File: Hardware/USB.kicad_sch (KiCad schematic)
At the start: 24 parts, among them Q1 MBT3904DW1, U3 CH340C, U9 USB251xB, Y3 24MHz

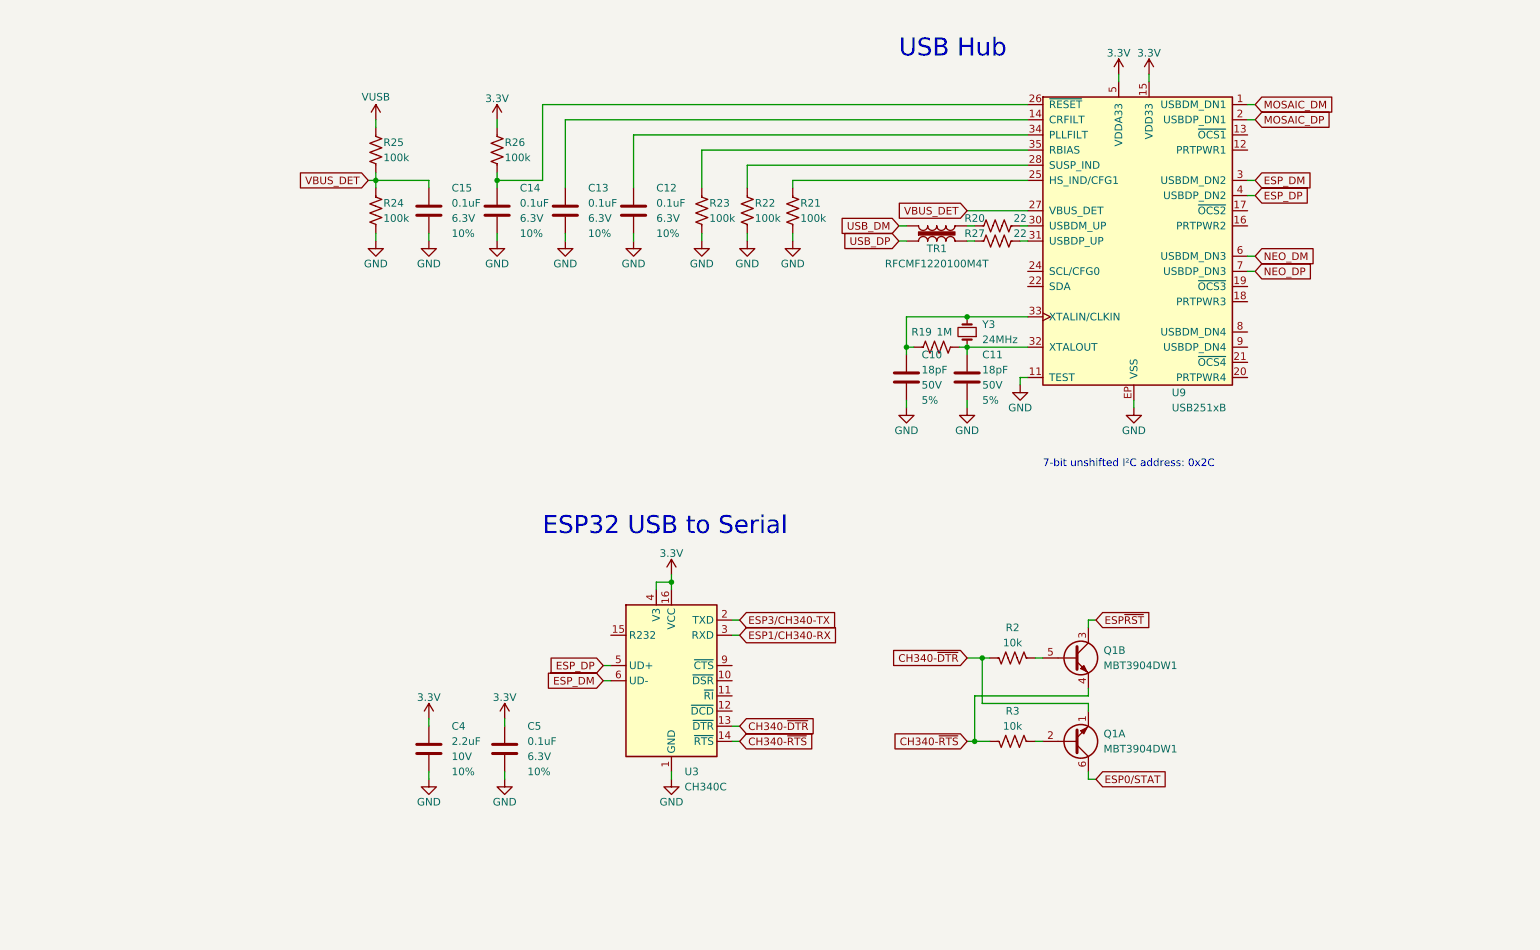
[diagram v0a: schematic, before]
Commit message: Schematic updates
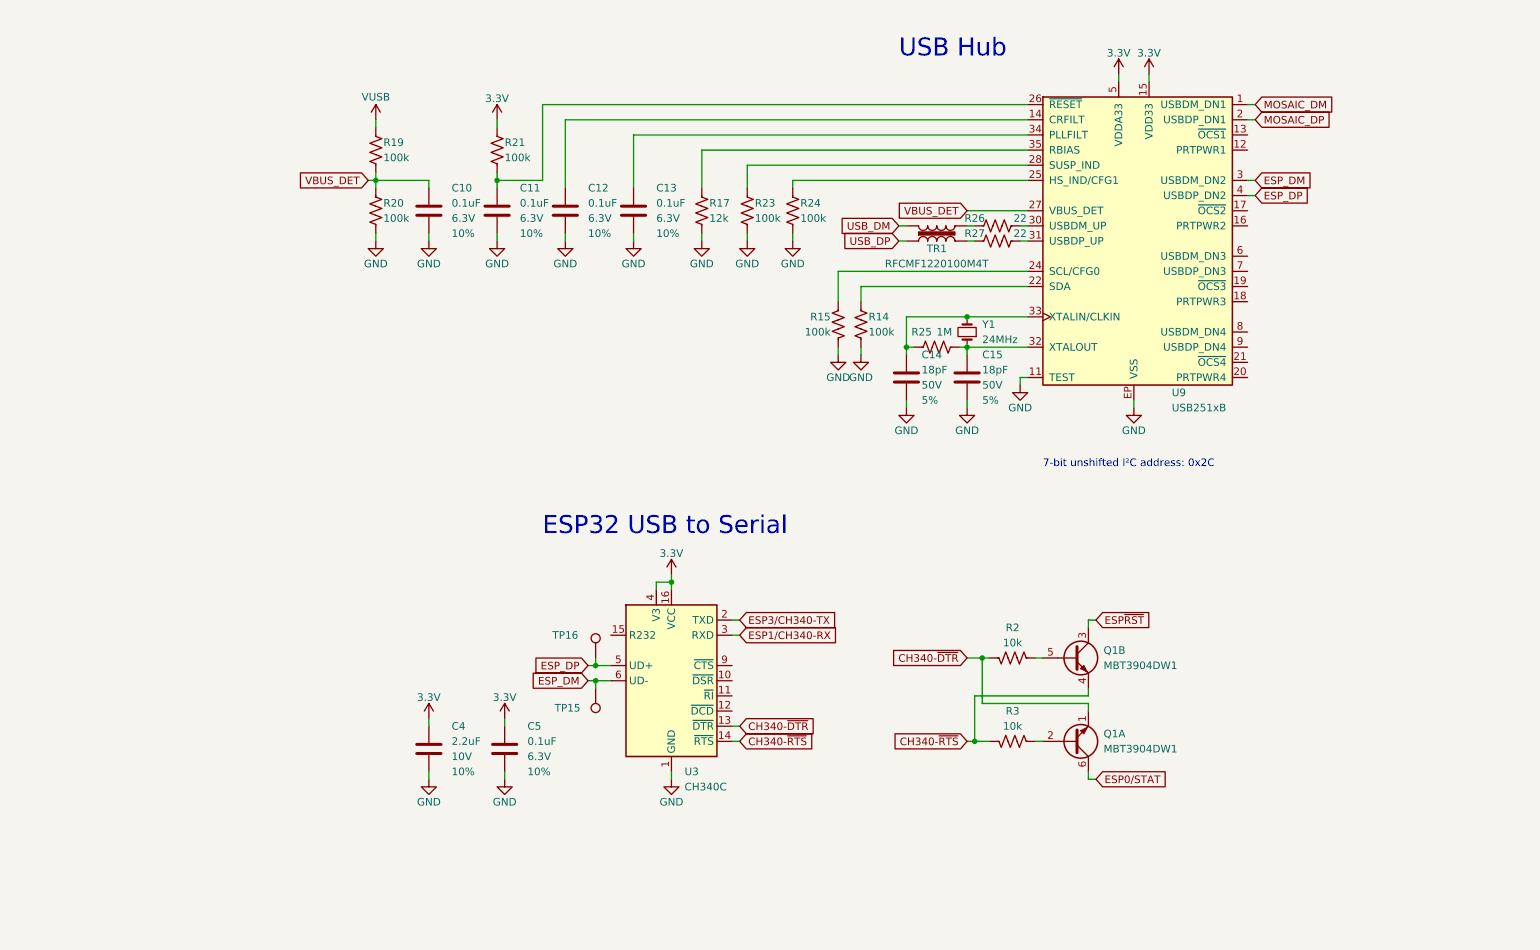
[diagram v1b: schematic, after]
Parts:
- removed R23: 100k, SparkFun-Resistor:R_0402_1005Metric, symbol SparkFun-Resistor:100k_0402
- added R14, R15: 100k, SparkFun-Resistor:R_0402_1005Metric, symbol SparkFun-Resistor:100k_0402
- added R17: 12k, SparkFun-Resistor:R_0402_1005Metric, symbol SparkFun-Resistor:12k_0402
- added TP15, TP16: PTH, SparkFun-Connector:1X01, symbol SparkFun-Connector:TestPoint_PTH
- renumbered C15 to C10, C14 to C11, C13 to C12, C12 to C13, C10 to C14, C11 to C15, R25 to R19, R24 to R20, R26 to R21, R22 to R23, R21 to R24, R19 to R25, R20 to R26, Y3 to Y1
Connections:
- net ESP_DM: now also TP15.1
- net ESP_DP: now also TP16.1
- net GND: now also R14.2, R15.2, R17.1
- net at U9.35 (RBIAS): now also R17.2
- net at U9.22 (SDA): now also R14.1
- net at U9.24 (SCL/CFG0): now also R15.1
- net NEO_DM: no longer names the net of U9.6 (USBDM_DN3)
- net NEO_DP: no longer names the net of U9.7 (USBDP_DN3)

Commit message: Ready for airwire review
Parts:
- Y1: PROD_ID XTAL- -> XTAL-14845
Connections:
- net ESP0/STAT renamed ESP0/BOOT
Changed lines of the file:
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@@
     )
   )
-  (global_label "ESP0{slash}STAT" (shape input) (at 194.31 146.05 0) (fields_autoplaced)
+  (global_label "ESP0{slash}BOOT" (shape input) (at 194.31 146.05 0) (fields_autoplaced)
     (effects (font (size 1.27 1.27)) (justify left))
     (property "Intersheetrefs" "${INTERSHEET_REFS}" (at 207.697 146.05 0)
@@
       (effects (font (size 1.27 1.27)) hide)
     )
-    (property "PROD_ID" "XTAL-" (at 182.88 71.12 0)
-      (effects (font (size 1.27 1.27)) hide)
-    )
+    (property "PROD_ID" "XTAL-14845" (at 182.88 71.12 0)
+      (effects (font (size 1.27 1.27)) hide)
+    )

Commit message: Work in progress...
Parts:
- removed TP15, TP16: PTH, SparkFun-Connector:1X01, symbol SparkFun-Connector:TestPoint_PTH
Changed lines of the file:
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@@
   (junction (at 93.98 45.72) (diameter 0) (color 0 0 0 0)
   )
-  (junction (at 110.49 129.54) (diameter 0) (color 0 0 0 0)
-  )
   (junction (at 173.99 139.7) (diameter 0) (color 0 0 0 0)
   )
@@
   (junction (at 162.56 73.66) (diameter 0) (color 0 0 0 0)
   )
-  (junction (at 110.49 127) (diameter 0) (color 0 0 0 0)
-  )
   (junction (at 123.19 113.03) (diameter 0) (color 0 0 0 0)
   )
@@
     (stroke (width 0) (type default))
   )
-  (wire (pts (xy 110.49 125.73) (xy 110.49 127))
-    (stroke (width 0) (type default))
-  )
   (wire (pts (xy 182.88 38.1) (xy 116.84 38.1))
     (stroke (width 0) (type default))
@@
     (stroke (width 0) (type default))
   )
-  (wire (pts (xy 110.49 129.54) (xy 113.03 129.54))
-    (stroke (width 0) (type default))
-  )
   (wire (pts (xy 82.55 137.16) (xy 82.55 135.89))
     (stroke (width 0) (type default))
@@
     (stroke (width 0) (type default))
   )
-  (wire (pts (xy 109.22 127) (xy 110.49 127))
-    (stroke (width 0) (type default))
-  )
   (wire (pts (xy 181.61 78.74) (xy 181.61 80.01))
     (stroke (width 0) (type default))
@@
     (stroke (width 0) (type default))
   )
-  (wire (pts (xy 109.22 129.54) (xy 110.49 129.54))
+  (wire (pts (xy 111.76 129.54) (xy 113.03 129.54))
     (stroke (width 0) (type default))
   )
@@
     (stroke (width 0) (type default))
   )
-  (wire (pts (xy 110.49 129.54) (xy 110.49 130.81))
-    (stroke (width 0) (type default))
-  )
-  (wire (pts (xy 110.49 127) (xy 113.03 127))
+  (wire (pts (xy 111.76 127) (xy 113.03 127))
     (stroke (width 0) (type default))
   )
@@
     )
   )
-  (global_label "ESP_DM" (shape input) (at 109.22 129.54 180) (fields_autoplaced)
+  (global_label "ESP_DM" (shape input) (at 111.76 129.54 180) (fields_autoplaced)
     (effects (font (size 1.27 1.27)) (justify right))
-    (property "Intersheetrefs" "${INTERSHEET_REFS}" (at 98.9173 129.54 0)
+    (property "Intersheetrefs" "${INTERSHEET_REFS}" (at 101.4573 129.54 0)
       (effects (font (size 1.27 1.27)) (justify right) hide)
     )
   )
-  (global_label "ESP_DP" (shape input) (at 109.22 127 180) (fields_autoplaced)
+  (global_label "ESP_DP" (shape input) (at 111.76 127 180) (fields_autoplaced)
     (effects (font (size 1.27 1.27)) (justify right))
-    (property "Intersheetrefs" "${INTERSHEET_REFS}" (at 99.0987 127 0)
+    (property "Intersheetrefs" "${INTERSHEET_REFS}" (at 101.6387 127 0)
       (effects (font (size 1.27 1.27)) (justify right) hide)
     )
@@
         (path "/e3dd3ae4-244d-4cba-9cca-5d2abf83f29a/0cda3e5b-c4bb-4a16-94d7-679fa3b0b0b8"
           (reference "C5") (unit 1)
-        )
-      )
-    )
-  )
-  (symbol (lib_id "SparkFun-Connector:TestPoint_PTH") (at 110.49 130.81 180) (unit 1)
-    (in_bom yes) (on_board yes) (dnp no) (fields_autoplaced)
-    (property "Reference" "TP15" (at 107.95 134.112 0)
-      (effects (font (size 1.27 1.27)) (justify left))
-    )
-    (property "Value" "PTH" (at 110.49 127 0)
-      (effects (font (size 1.27 1.27)) hide)
-    )
-    (property "Footprint" "SparkFun-Connector:1X01" (at 111.76 124.46 0)
-      (effects (font (size 1.27 1.27)) hide)
-    )
-    (property "Datasheet" "~" (at 110.49 123.19 0)
-      (effects (font (size 1.27 1.27)) hide)
-    )
-    (pin "1")
-    (instances
-      (project "SparkFun_RTK_Facet_mosaic"
-        (path "/e3dd3ae4-244d-4cba-9cca-5d2abf83f29a/0cda3e5b-c4bb-4a16-94d7-679fa3b0b0b8"
-          (reference "TP15") (unit 1)
         )
       )
@@
         )
       )
-    )
-  )
-  (symbol (lib_id "SparkFun-Connector:TestPoint_PTH") (at 110.49 125.73 0) (unit 1)
-    (in_bom yes) (on_board yes) (dnp no)
-    (property "Reference" "TP16" (at 105.41 121.92 0)
-      (effects (font (size 1.27 1.27)))
-    )
-    (property "Value" "PTH" (at 110.49 129.54 0)
-      (effects (font (size 1.27 1.27)) hide)
-    )
-    (property "Footprint" "SparkFun-Connector:1X01" (at 109.22 132.08 0)
-      (effects (font (size 1.27 1.27)) hide)
-    )
-    (property "Datasheet" "~" (at 110.49 133.35 0)
-      (effects (font (size 1.27 1.27)) hide)
-    )
-    (pin "1")
-    (instances
-      (project "SparkFun_RTK_Facet_mosaic"
-        (path "/e3dd3ae4-244d-4cba-9cca-5d2abf83f29a/0cda3e5b-c4bb-4a16-94d7-679fa3b0b0b8"
-          (reference "TP16") (unit 1)
-        )
-      )

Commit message: Routed
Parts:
- added TP19, TP20: 1.0mm, SparkFun-Connector:TestPoint-1.0mm, symbol SparkFun-Connector:TestPoint_1.0mm
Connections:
- net USB_DM: now also TP19.1
- net USB_DP: now also TP20.1
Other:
- moved on the sheet: C14, C15, R14, R15, R25, R26, R27, TR1, U9, Y1

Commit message: Nudge things on USB schematic
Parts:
- added C30: 0.1uF, SparkFun-Capacitor:C_0402_1005Metric, symbol SparkFun-Capacitor:0.1uF_0402_6.3V_10%
- added C9: 2.2uF, SparkFun-Capacitor:C_0402_1005Metric, symbol SparkFun-Capacitor:2.2uF_0402_10V_10%
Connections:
- net 3.3V: now also C30.1, C9.1
- net GND: now also C30.2, C9.2
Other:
- moved on the sheet: C10, C11, C12, C13, C14, C15, R14, R15, R17, R19, R20, R21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

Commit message: v1.1 routed
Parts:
- U3: footprint SparkFun-Semiconductor-Standard:SO16 -> SparkFun-Semiconductor-Standard:SO-16
- Y1: footprint SparkFun-Clock:CRYSTAL-SMD-2.0X1.6MM -> SparkFun-Clock:Crystal_SMD_2.0x1.6mm
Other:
- moved on the sheet: C10, C11, C12, C13, C14, C15, C30, C4, C5, C9, Q1A, Q1B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

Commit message: v1.2 routed
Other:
- title: (none) -> USB
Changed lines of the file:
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@@
 	(generator_version "8.0")
 	(paper "USLetter")
+	(title_block
+		(title "USB")
+	)
 	(junction
 		(at 45.72 44.45)
@@
 			)
 		)
-		(property "Description" ""
+		(property "Description" "USB Transformer"
 			(at 144.78 53.34 0)
 			(effects
